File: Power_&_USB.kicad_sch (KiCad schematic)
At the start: 26 parts, among them J5 USB4745-03-A, U12 SN74LVC1T45DCK, U4 FT232HPQ, U6 SN74AXC4T774RSVR

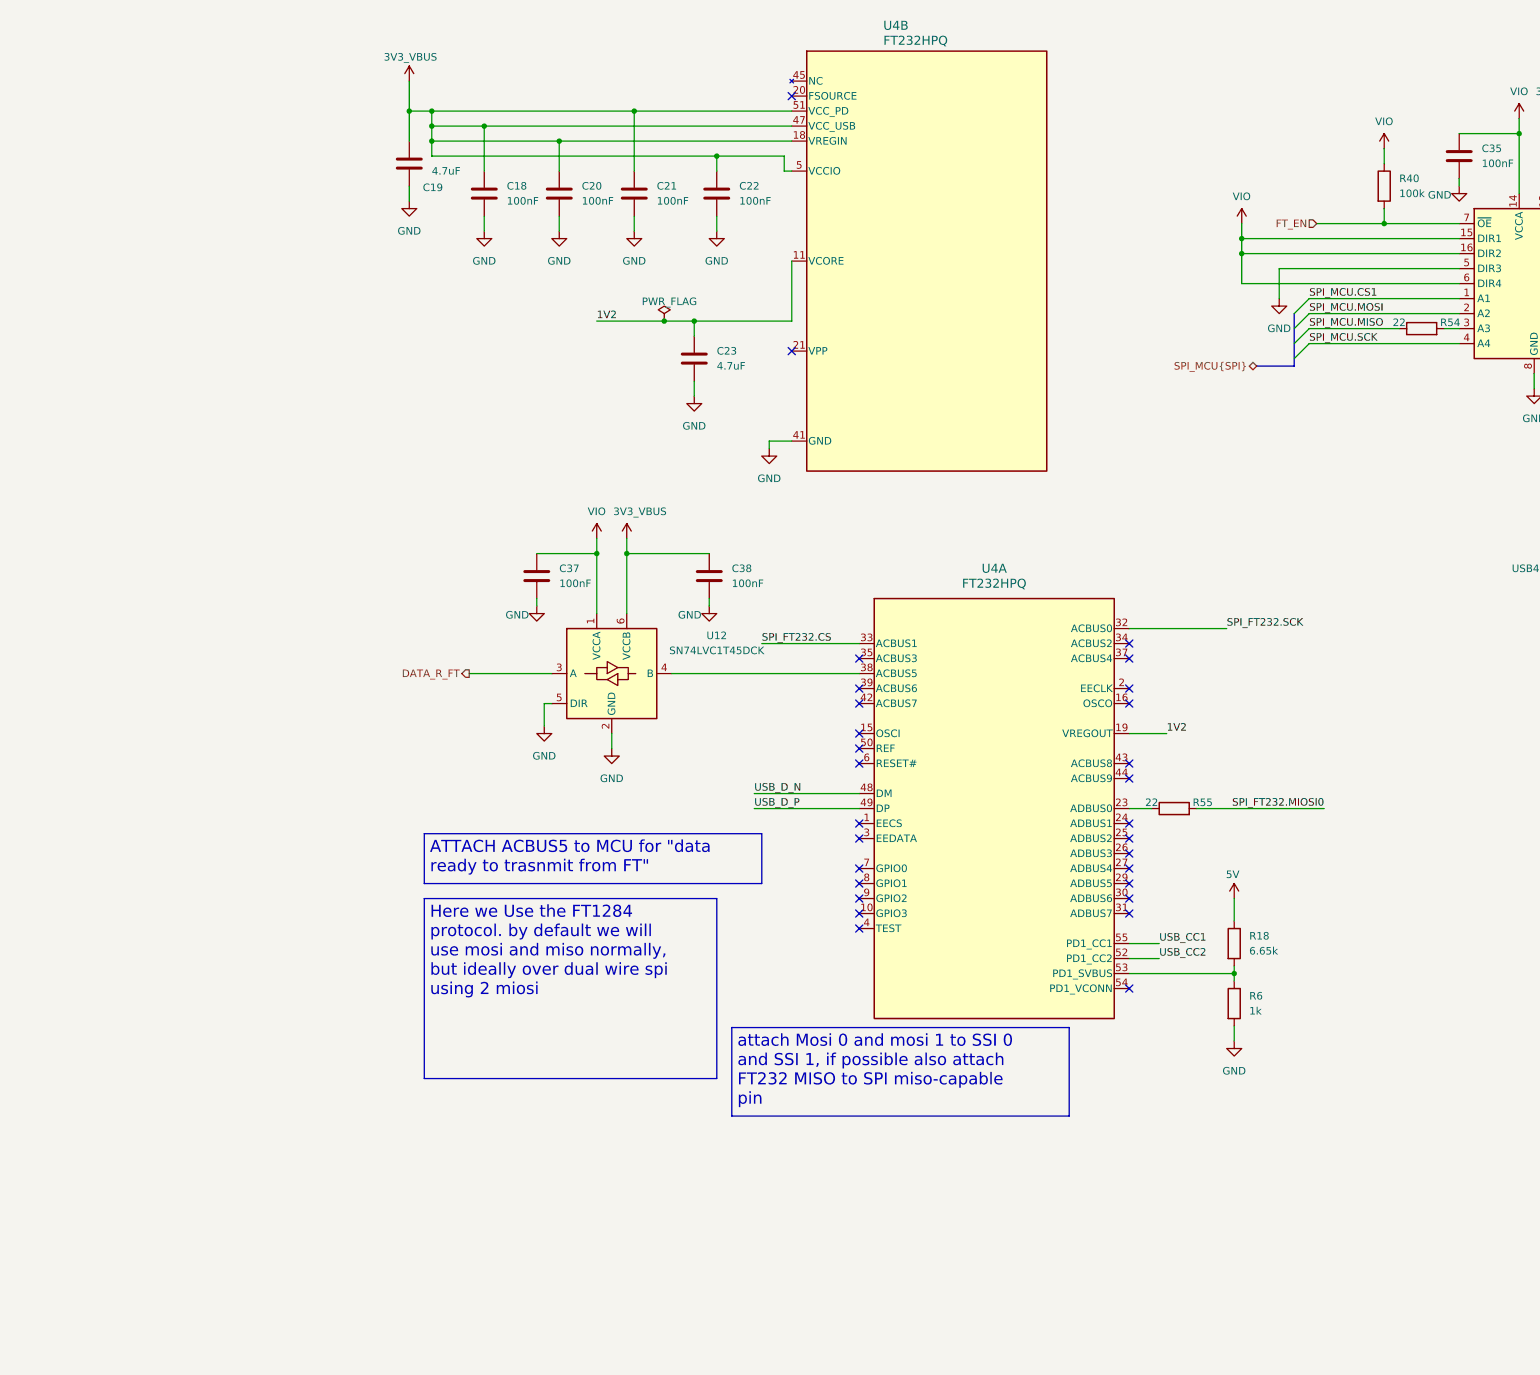
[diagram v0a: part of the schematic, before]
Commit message: updated eeprom and oscillator
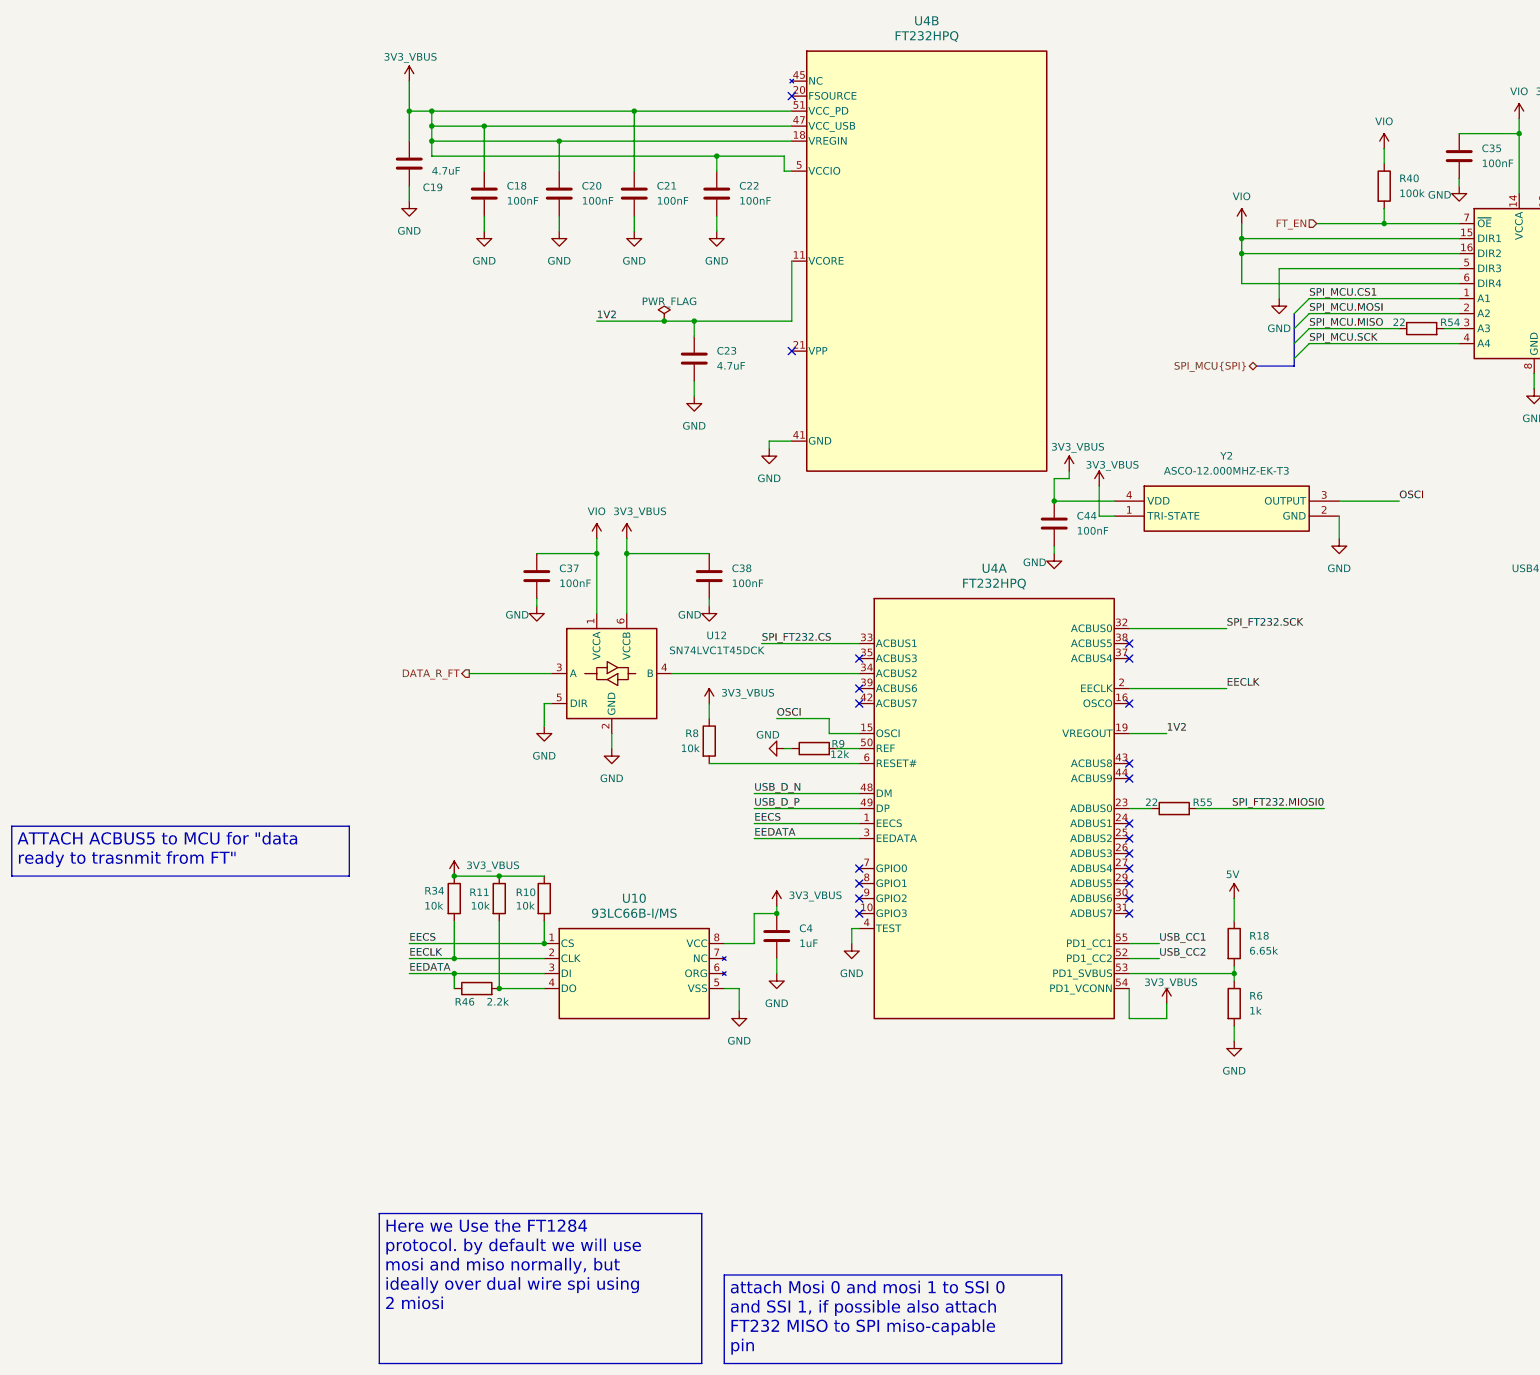
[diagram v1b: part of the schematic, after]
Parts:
- added C4: 1uF, Capacitor_SMD:C_0201_0603Metric, symbol #dzdb:g_cap/C-1u-0201
- added C44: 100nF, Capacitor_SMD:C_0201_0603Metric, symbol #dzdb:g_cap/C-100n-0201
- added R10, R11, R34, R8: 10k, Resistor_SMD:R_0201_0603Metric, symbol #dzdb:g_res/R-10K-0201
- added R46: 2.2k, Resistor_SMD:R_0201_0603Metric, symbol #dzdb:g_res/R-2K2-0201
- added R9: 12k, Resistor_SMD:R_0201_0603Metric, symbol #dzdb:g_res/R-12K-0201
- added U10: 93LC66B-I/MS, dz_mem:MSOP8_MC_MCH, symbol #dzdb:s_mem/IC-EEPROM-93LC66B-I/MS
- added Y2: ASCO-12.000MHZ-EK-T3, dz_comm:ASCO16000MHZEKT, symbol #dzdb:s_clk/XTL-ABR-ASCO-12M
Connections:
- net 3V3_VBUS: now also U4.54 (PD1_VCONN), C4.1, C44.1, R10.1, R11.1, R34.1, R8.1, U10.8 (VCC), Y2.1 (TRI-STATE), Y2.4 (VDD)
- net GND: now also U4.4 (TEST), C4.2, C44.2, R9.1, U10.5 (VSS), Y2.2 (GND)
- net at U12.4 (B): now also U4.34 (ACBUS2); no longer U4.38 (ACBUS5)
- net EECS: now reaches U4.1 (EECS)
- net EECS: now also R10.2, U10.1 (CS)
- net OSCI: now reaches U4.15 (OSCI)
- net OSCI: now also Y2.3 (OUTPUT)
- net EECLK: now reaches U4.2 (EECLK)
- net EECLK: now also R34.2, U10.2 (CLK)
- net EEDATA: now reaches U4.3 (EEDATA)
- net EEDATA: now also R46.1, U10.3 (DI)
- net at U4.50 (REF): now also R9.2
- net at U4.6 (RESET#): now also R8.2
- new net: R11.2, R46.2, U10.4 (DO)
- no-connect marks 39 -> 31

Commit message: updated schematic and PCB
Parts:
- added U11: 93LCxxA, Package_SO:SOIC-8_3.9x4.9mm_P1.27mm, symbol Memory_EEPROM:93LCxxA
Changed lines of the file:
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@@
+	)
+	(symbol
+		(lib_id "Memory_EEPROM:93LCxxA")
+		(at 54.61 184.15 0)
+		(unit 1)
+		(body_style 1)
+		(exclude_from_sim no)
+		(in_bom yes)
+		(on_board yes)
+		(in_pos_files yes)
+		(dnp no)
+		(fields_autoplaced yes)
+		(property "Reference" "U11"
+			(at 56.7533 173.99 0)
+			(show_name no)
+			(do_not_autoplace no)
+			(effects
+				(font
+					(size 1.27 1.27)
+				)
+				(justify left)
+			)
+		)
+		(property "Value" "93LCxxA"
+			(at 56.7533 176.53 0)
+			(show_name no)
+			(do_not_autoplace no)
+			(effects
+				(font
+					(size 1.27 1.27)
+				)
+				(justify left)
+			)
+		)
+		(property "Footprint" "Package_SO:SOIC-8_3.9x4.9mm_P1.27mm"
+			(at 54.61 184.15 0)
+			(hide yes)
+			(show_name no)
+			(do_not_autoplace no)
+			(effects
+				(font
+					(size 1.27 1.27)
+				)
+			)
+		)
+		(property "Datasheet" "http://ww1.microchip.com/downloads/en/DeviceDoc/20001749K.pdf"
+			(at 54.61 184.15 0)
+			(hide yes)
+			(show_name no)
+			(do_not_autoplace no)
+			(effects
+				(font
+					(size 1.27 1.27)
+				)
+			)
+		)
+		(property "Description" "Serial EEPROM, 93 Series, 2.5V, DIP-8/SOIC-8"
+			(at 54.61 184.15 0)
+			(hide yes)
+			(show_name no)
+			(do_not_autoplace no)
+			(effects
+				(font
+					(size 1.27 1.27)
+				)
+			)
+		)
+		(pin "1"
+		)
+		(pin "7"
+		)
+		(pin "6"
+		)
+		(pin "2"
+		)
+		(pin "5"
+		)
+		(pin "3"
+		)
+		(pin "4"
+		)
+		(pin "8"
+		)
+		(instances
+			(project "wius_new"
+				(path "/8543d6cf-82a6-4fc5-8760-a0773a1d6e4c/f56cbe0a-9129-41bf-b268-cb28a87edbe6"
+					(reference "U11")
+					(unit 1)
+				)
+			)
+		)
 	)
 	(symbol

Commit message: updated routing
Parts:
- removed U11: 93LCxxA, Package_SO:SOIC-8_3.9x4.9mm_P1.27mm, symbol Memory_EEPROM:93LCxxA
- Y2: footprint dz_comm:ASCO16000MHZEKT -> Oscillator:Oscillator_SMD_Abracon_ASCO-4Pin_1.6x1.2mm
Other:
- moved on the sheet: C4, R10, R11, R34, R46
